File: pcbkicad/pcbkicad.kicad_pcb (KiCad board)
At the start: 2 copper layers, 38 parts, among them J1 USBDaughterboard, U1 AMS1117-3.3, U2 STM32F072CBTx

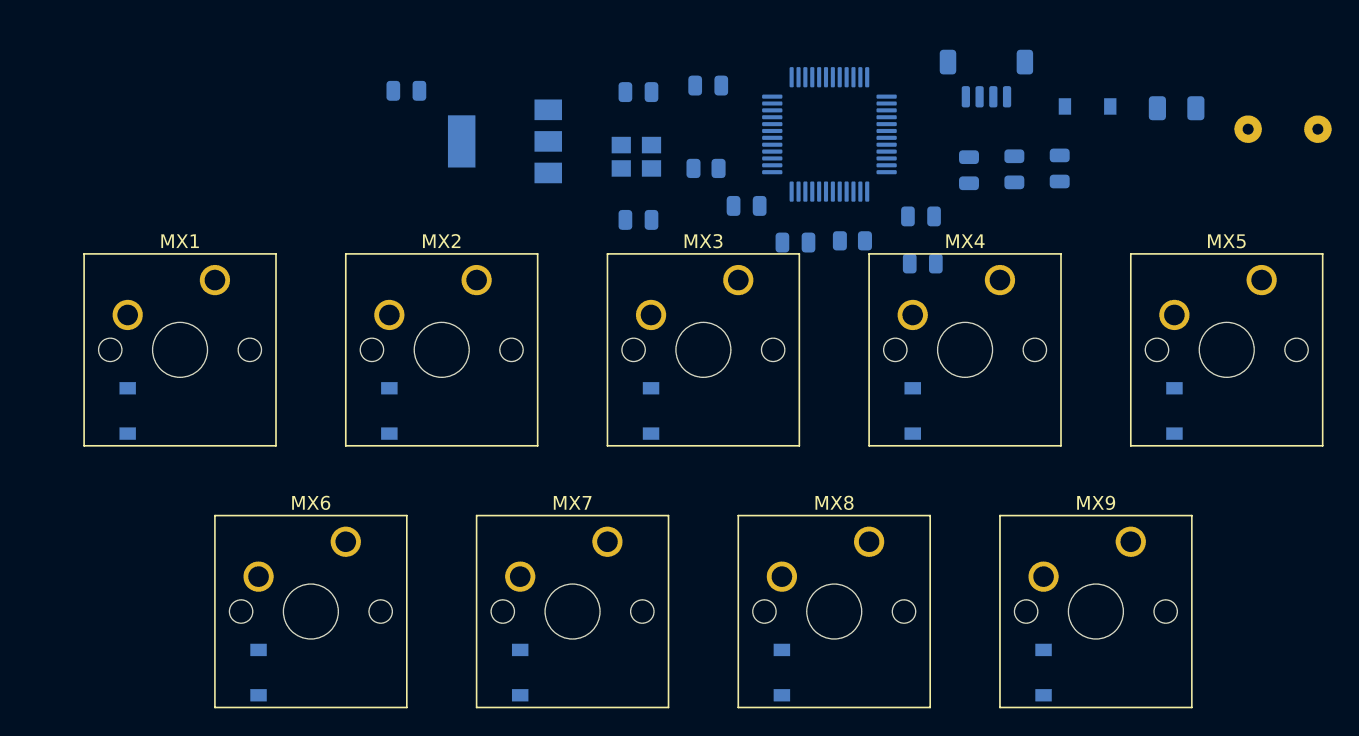
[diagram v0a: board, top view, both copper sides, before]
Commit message: First attempt at routing
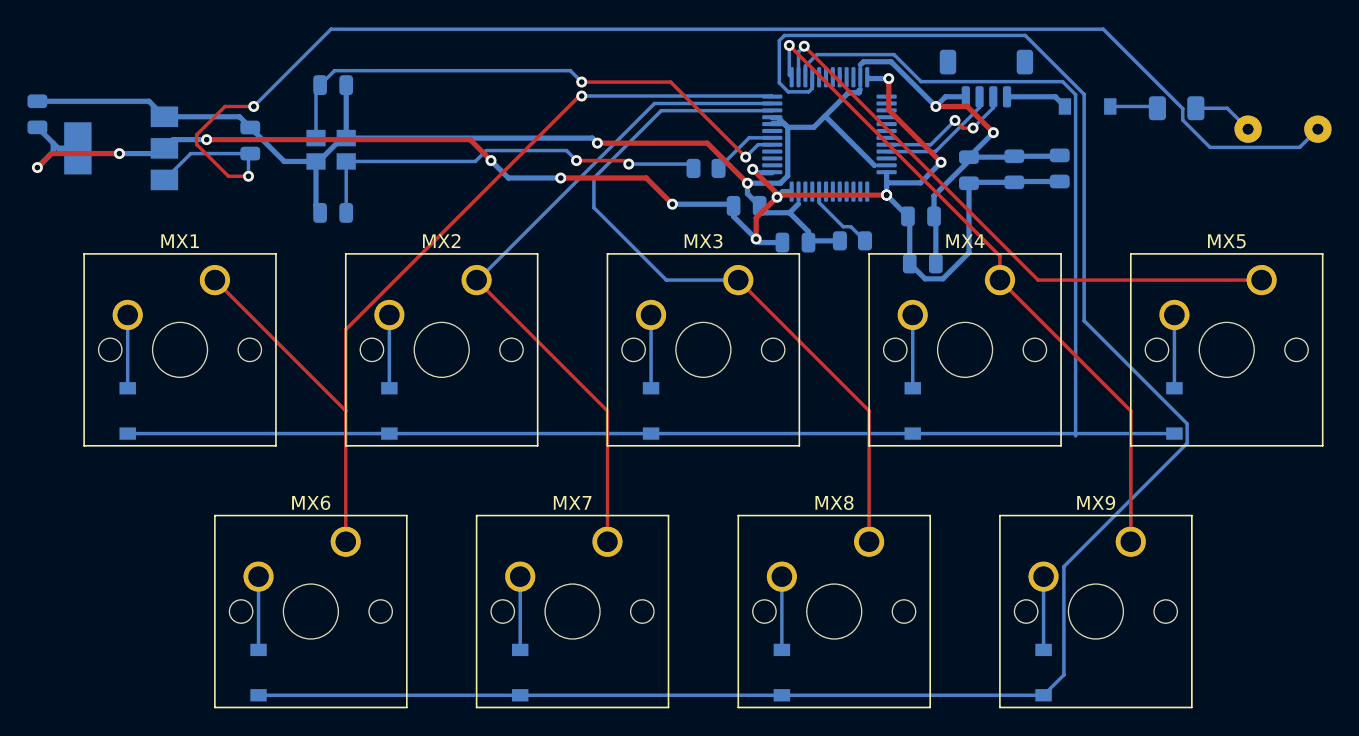
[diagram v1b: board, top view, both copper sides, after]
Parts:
- moved C1 33.6 mm to (93.9, 26.4), turned to 90 degrees
- moved U1 27.9 mm to (84.5, 26.9)
- moved C10 26.9 mm to (78.4, 24.4), turned to 270 degrees
- moved C3 22.2 mm to (99.9, 22.3)
- moved C4 22.2 mm to (99.9, 31.6)
- moved HSE1 22.2 mm to (99.7, 27.0)
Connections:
- U2 pad 10: COL0 -> COL2
- U2 pad 12: COL2 -> COL0
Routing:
- net ROW1: track 0.00 -> 139.1 mm
- net GND: track 0.00 -> 127.3 mm, vias 0 -> 4
- net ROW0: track 0.00 -> 123.1 mm
- net +3V3: track 0.00 -> 121.4 mm, vias 0 -> 13
- net Net-(C1-Pad1): track 0.00 -> 103.6 mm, vias 0 -> 2
- net COL0: track 0.00 -> 67.0 mm, vias 0 -> 1
- net COL2: track 0.00 -> 52.9 mm
- net COL1: track 0.00 -> 49.8 mm
- net COL3: track 0.00 -> 48.8 mm, vias 0 -> 1
- net COL4: track 0.00 -> 42.8 mm, vias 0 -> 1
- net HSE_in: track 0.00 -> 40.3 mm, vias 0 -> 2
- net Net-(C4-Pad1): track 0.00 -> 29.9 mm, vias 0 -> 2
- net D-: track 0.00 -> 10.3 mm, vias 0 -> 2
- net D+: track 0.00 -> 8.87 mm
- net Net-(D9-Pad2): track 0.00 -> 5.34 mm
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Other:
- net class Default: trace_width 0.25 -> 0.254
- net class Power added: clearance 0.2, trace_width 0.381, via_dia 0.8, via_drill 0.4

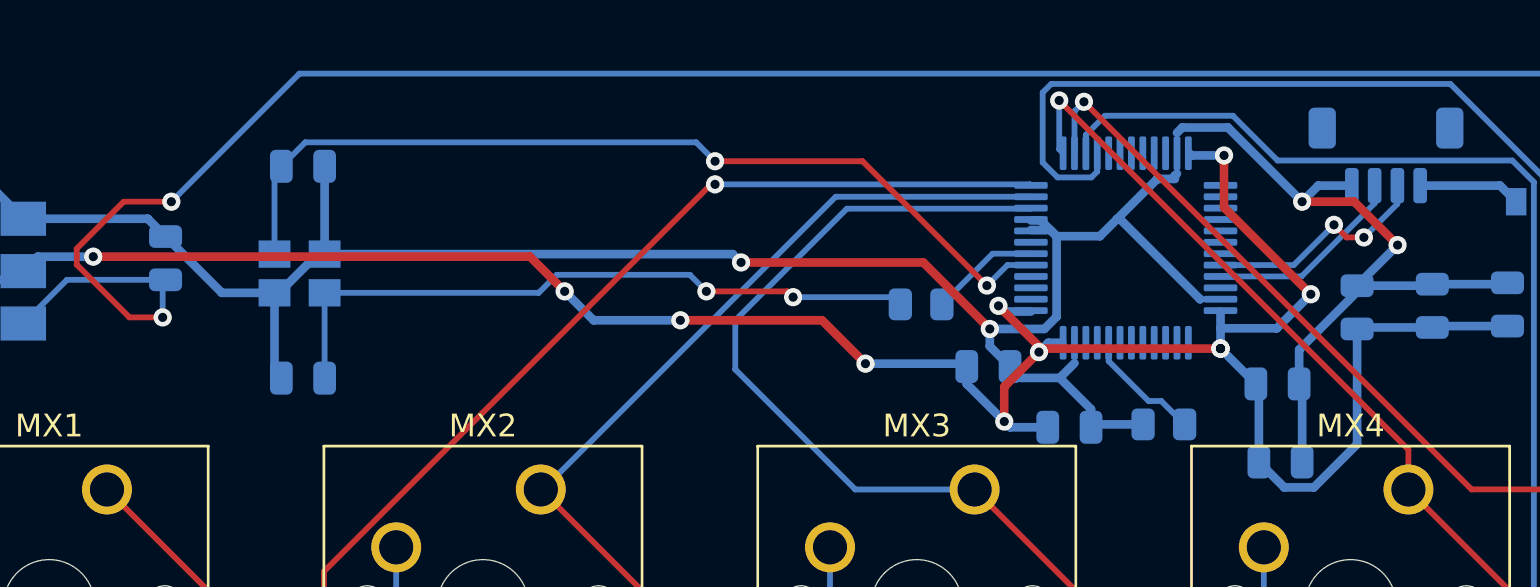
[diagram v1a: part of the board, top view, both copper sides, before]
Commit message: Ground fill
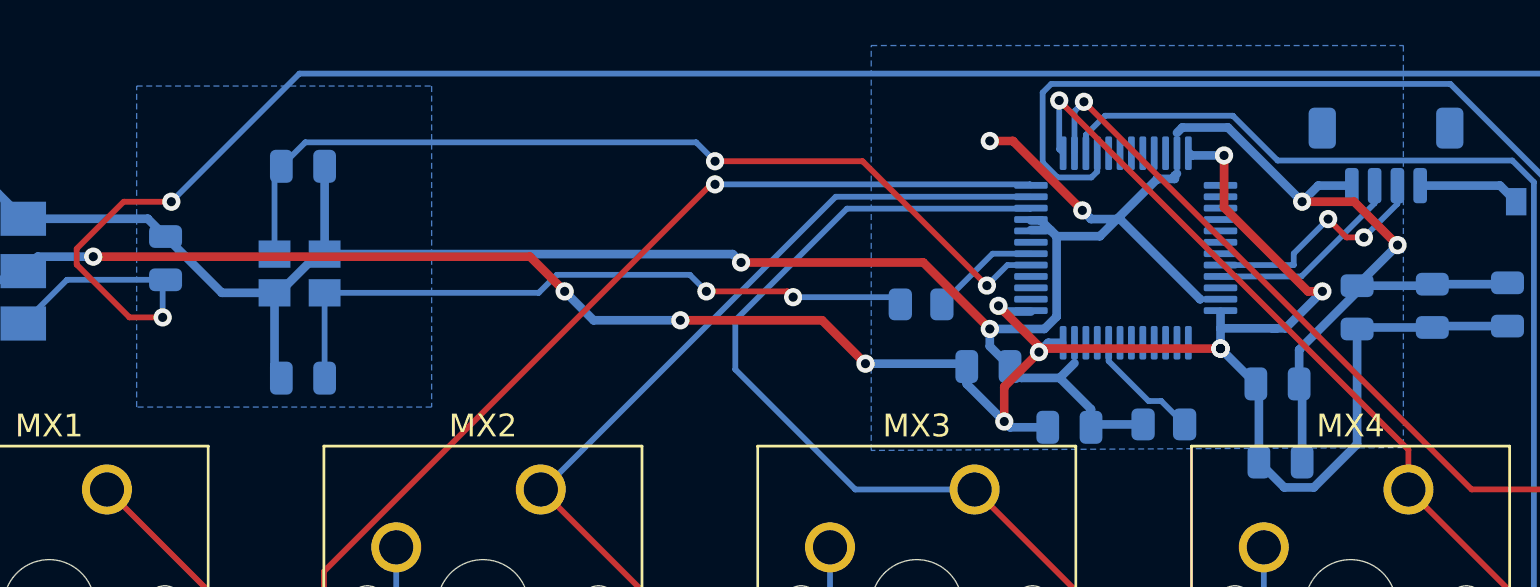
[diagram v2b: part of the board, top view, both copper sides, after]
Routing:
- net GND: track 127.3 -> 134.3 mm, vias 4 -> 6
- net +3V3: track 121.4 -> 122.6 mm
- added copper zone on B.Cu, net GND
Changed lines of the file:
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@@
     (thickness 1.6)
     (drawings 0)
-    (tracks 268)
+    (tracks 278)
     (zones 0)
     (modules 38)
@@
   (segment (start 135.763 24.638) (end 139.283 28.158) (width 0.381) (layer B.Cu) (net 1))
   (segment (start 135.636 24.638) (end 135.763 24.638) (width 0.381) (layer B.Cu) (net 1))
-  (segment (start 134.883822 25.390178) (end 135.636 24.638) (width 0.381) (layer B.Cu) (net 1))
   (segment (start 135.636 24.638) (end 137.40049 22.87351) (width 0.381) (layer B.Cu) (net 1))
   (segment (start 143.764 32.009) (end 143.632 31.877) (width 0.381) (layer B.Cu) (net 1))
@@
   (segment (start 132.290842 24.69851) (end 131.8545 24.69851) (width 0.381) (layer B.Cu) (net 1))
   (segment (start 132.98251 25.390178) (end 132.290842 24.69851) (width 0.381) (layer B.Cu) (net 1))
+  (segment (start 134.883822 25.390178) (end 135.636 24.638) (width 0.381) (layer B.Cu) (net 1))
+  (via (at 134.112 24.257) (size 0.8) (drill 0.4) (layers F.Cu B.Cu) (net 1))
+  (segment (start 134.493 24.638) (end 134.112 24.257) (width 0.381) (layer B.Cu) (net 1))
+  (segment (start 135.636 24.638) (end 134.493 24.638) (width 0.381) (layer B.Cu) (net 1))
+  (via (at 130.048 21.209) (size 0.8) (drill 0.4) (layers F.Cu B.Cu) (net 1))
+  (segment (start 131.064 21.209) (end 130.048 21.209) (width 0.381) (layer F.Cu) (net 1))
+  (segment (start 134.112 24.257) (end 131.064 21.209) (width 0.381) (layer F.Cu) (net 1))
   (segment (start 89.524 27.305) (end 87.605 29.224) (width 0.254) (layer B.Cu) (net 2))
   (segment (start 93.853 27.305) (end 89.524 27.305) (width 0.254) (layer B.Cu) (net 2))
@@
   (segment (start 146.177 34.52382) (end 144.27931 36.42151) (width 0.381) (layer B.Cu) (net 3))
   (segment (start 146.177 29.464) (end 146.177 34.52382) (width 0.381) (layer B.Cu) (net 3))
-  (via (at 144.145 27.94) (size 0.8) (drill 0.4) (layers F.Cu B.Cu) (net 3))
-  (segment (start 142.6495 29.4355) (end 144.145 27.94) (width 0.381) (layer B.Cu) (net 3))
-  (segment (start 140.1795 29.4355) (end 142.6495 29.4355) (width 0.381) (layer B.Cu) (net 3))
+  (via (at 144.653 27.813) (size 0.8) (drill 0.4) (layers F.Cu B.Cu) (net 3))
   (segment (start 140.1795 30.3245) (end 140.1795 29.4355) (width 0.381) (layer B.Cu) (net 3))
   (segment (start 140.1795 29.4355) (end 140.1795 28.69851) (width 0.381) (layer B.Cu) (net 3))
   (via (at 140.335 21.844) (size 0.8) (drill 0.4) (layers F.Cu B.Cu) (net 3))
   (segment (start 140.335 24.13) (end 140.335 21.844) (width 0.381) (layer F.Cu) (net 3))
-  (segment (start 144.145 27.94) (end 140.335 24.13) (width 0.381) (layer F.Cu) (net 3))
   (segment (start 138.90601 21.844) (end 138.80751 21.7455) (width 0.381) (layer B.Cu) (net 3))
   (segment (start 140.335 21.844) (end 138.90601 21.844) (width 0.381) (layer B.Cu) (net 3))
@@
   (segment (start 132.3625 30.3245) (end 132.207 30.48) (width 0.381) (layer F.Cu) (net 3))
   (segment (start 140.1795 30.3245) (end 132.3625 30.3245) (width 0.381) (layer F.Cu) (net 3))
+  (segment (start 143.0305 29.4355) (end 142.4655 29.4355) (width 0.381) (layer B.Cu) (net 3))
+  (segment (start 144.653 27.813) (end 143.0305 29.4355) (width 0.381) (layer B.Cu) (net 3))
+  (segment (start 142.4655 29.4355) (end 142.6495 29.4355) (width 0.381) (layer B.Cu) (net 3))
+  (segment (start 140.1795 29.4355) (end 142.4655 29.4355) (width 0.381) (layer B.Cu) (net 3))
+  (segment (start 144.018 27.813) (end 140.335 24.13) (width 0.381) (layer F.Cu) (net 3))
+  (segment (start 144.653 27.813) (end 144.018 27.813) (width 0.381) (layer F.Cu) (net 3))
   (segment (start 98.638 22.62025) (end 98.938 22.32025) (width 0.254) (layer B.Cu) (net 4))
   (segment (start 98.638 26.1765) (end 98.638 22.62025) (width 0.254) (layer B.Cu) (net 4))
@@
   (segment (start 147.947 23.972134) (end 146.475067 25.444067) (width 0.254) (layer B.Cu) (net 21))
   (segment (start 147.947 23.169) (end 147.947 23.972134) (width 0.254) (layer B.Cu) (net 21))
-  (via (at 145.161 24.892) (size 0.8) (drill 0.4) (layers F.Cu B.Cu) (net 21))
-  (segment (start 145.713067 25.444067) (end 145.034 24.765) (width 0.254) (layer F.Cu) (net 21))
+  (via (at 144.907 24.638) (size 0.8) (drill 0.4) (layers F.Cu B.Cu) (net 21))
   (segment (start 146.475067 25.444067) (end 145.713067 25.444067) (width 0.254) (layer F.Cu) (net 21))
   (segment (start 143.395 26.658) (end 140.1795 26.658) (width 0.254) (layer B.Cu) (net 21))
-  (segment (start 145.161 24.892) (end 143.395 26.658) (width 0.254) (layer B.Cu) (net 21))
+  (segment (start 144.907 24.638) (end 145.713067 25.444067) (width 0.254) (layer F.Cu) (net 21))
+  (segment (start 143.395 26.15) (end 143.395 26.658) (width 0.254) (layer B.Cu) (net 21))
+  (segment (start 144.907 24.638) (end 143.395 26.15) (width 0.254) (layer B.Cu) (net 21))
   (segment (start 100.80625 46.0375) (end 91.28125 36.5125) (width 0.254) (layer F.Cu) (net 22))
   (segment (start 100.80625 55.5625) (end 100.80625 46.0375) (width 0.254) (layer F.Cu) (net 22))
@@
   (segment (start 135.267 30.876528) (end 137.018462 32.62799) (width 0.254) (layer B.Cu) (net 28))
   (segment (start 135.267 30.0705) (end 135.267 30.876528) (width 0.254) (layer B.Cu) (net 28))
+  (zone (net 1) (net_name GND) (layer B.Cu) (hatch edge 0.508)
+    (connect_pads (clearance 0.508))
+    (min_thickness 0.254)
+    (fill yes (arc_segments 32) (thermal_gap 0.508) (thermal_bridge_width 0.508) (smoothing chamfer))
+    (polygon
+      (pts
+        (xy 148.209 34.671) (xy 124.841 34.798) (xy 124.841 17.018) (xy 148.209 17.018)
+      )
+    )
+  )
+  (zone (net 1) (net_name GND) (layer B.Cu) (hatch edge 0.508)
+    (connect_pads (clearance 0.508))
+    (min_thickness 0.254)
+    (fill yes (arc_segments 32) (thermal_gap 0.508) (thermal_bridge_width 0.508) (smoothing chamfer))
+    (polygon
+      (pts
+        (xy 105.537 32.893) (xy 92.583 32.893) (xy 92.583 18.796) (xy 105.537 18.796)
+      )
+    )
+  )
 )

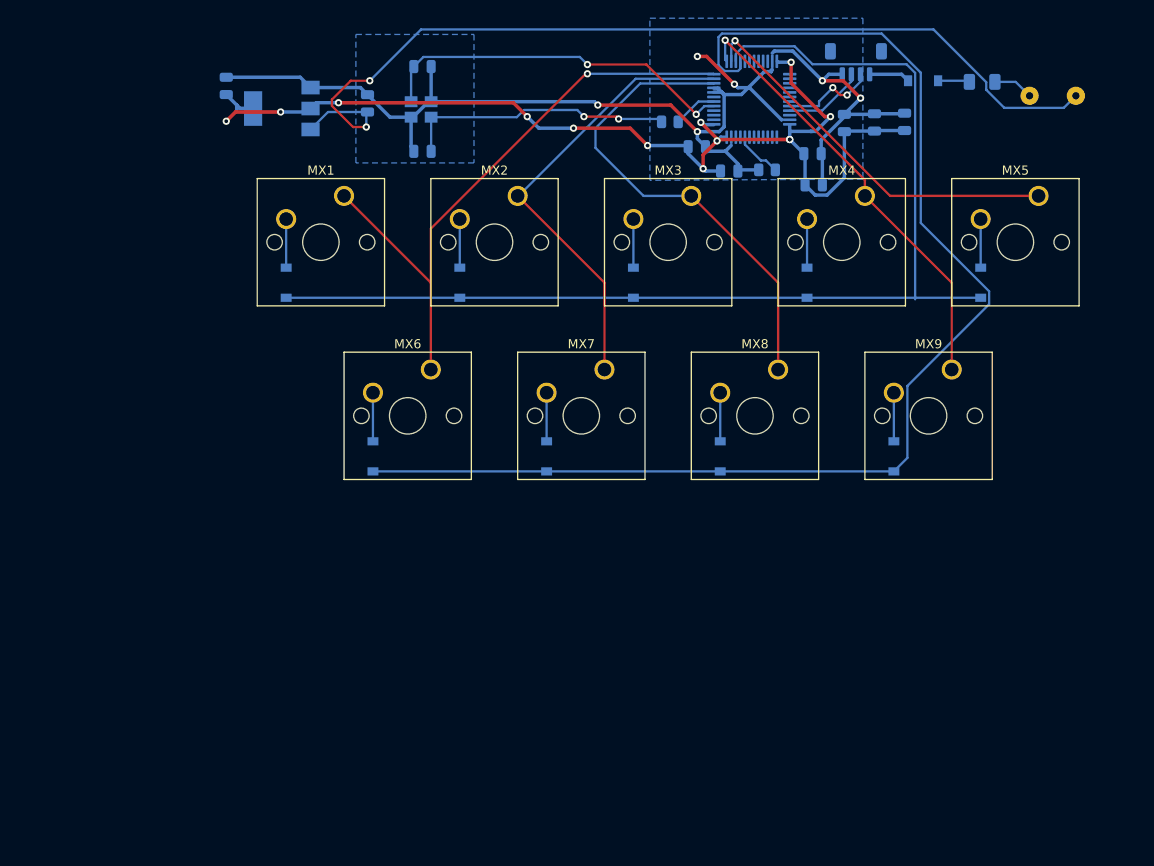
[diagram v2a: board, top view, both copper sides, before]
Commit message: Rerouted and removed unecessary elements
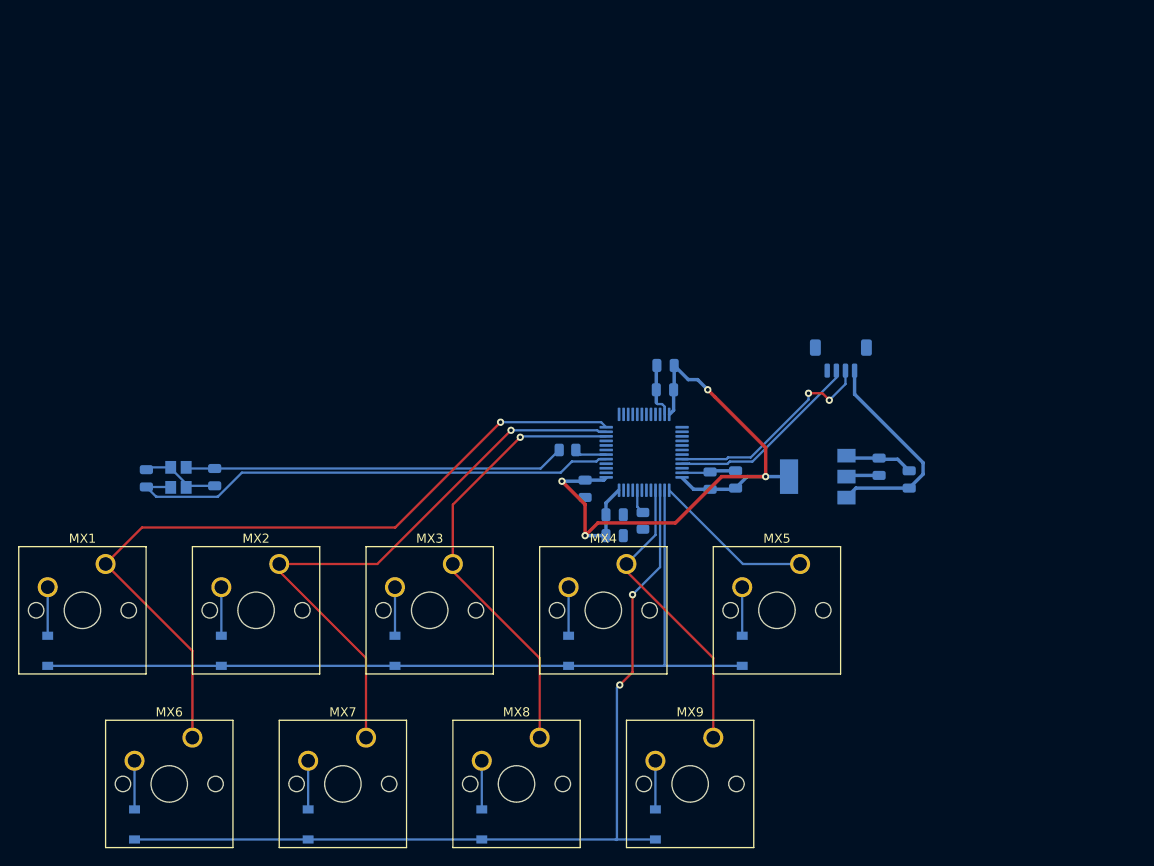
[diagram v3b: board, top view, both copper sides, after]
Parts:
- removed D1: B5819W, Diode_SMD:D_SOD-123
- removed F1: 500 mA, Fuse:Fuse_1206_3216Metric
- removed FB1: 100 @ 100 Mhz, Ferrite_THT:LairdTech_28C0236-0JW-10
- moved C1 72.4 mm to (153.3, 67.6)
- moved U1 71.3 mm to (143.3, 67.3)
- moved C10 68.5 mm to (131.4, 67.8)
- moved C3 54.4 mm to (69.6, 67.5), turned to 90 degrees
- moved C8 53.6 mm to (121.0, 73.8), turned to 180 degrees
- moved C6 49.8 mm to (121.0, 71.5), turned to 180 degrees
- moved HSE1 48.4 mm to (73.1, 67.4), turned to 90 degrees
- moved D2 48.1 mm to (58.8, 86.4)
- moved D3 48.1 mm to (77.8, 86.4)
- moved D4 48.1 mm to (96.9, 86.4)
- moved D5 48.1 mm to (115.9, 86.4)
- moved D6 48.1 mm to (135.0, 86.4)
- moved D9 48.1 mm to (106.4, 105.5)
- moved MX1 48.1 mm to (65.1, 76.9)
- moved MX4 48.1 mm to (122.3, 76.9)
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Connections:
- C1 pad 1: Net-(C1-Pad1) -> VCC
- U1 pad 3: Net-(C1-Pad1) -> VCC
- U2 pad 13: COL3 -> Net-(U2-Pad13)
- U2 pad 14: COL4 -> Net-(U2-Pad14)
- U2 pad 15: ROW0 -> Net-(U2-Pad15)
- U2 pad 16: ROW1 -> Net-(U2-Pad16)
- U2 pad 37: Net-(U2-Pad37) -> COL4
- U2 pad 38: Net-(U2-Pad38) -> ROW0
- U2 pad 39: Net-(U2-Pad39) -> ROW1
- U2 pad 40: Net-(U2-Pad40) -> COL3
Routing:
- net GND: track 134.3 -> 28.5 mm, vias 6 -> 0
- net Net-(C1-Pad1): track 103.6 -> 0.00 mm, vias 2 -> 0
- net ROW1: track 139.1 -> 97.5 mm, vias 0 -> 2
- net +3V3: track 122.6 -> 81.4 mm, vias 13 -> 4
- net ROW0: track 123.1 -> 95.5 mm
- net COL4: track 42.8 -> 17.7 mm, vias 1 -> 0
- net VCC: track 4.51 -> 24.0 mm
- net COL0: track 67.0 -> 84.6 mm
- net COL3: track 48.8 -> 32.4 mm, vias 1 -> 0
- net COL1: track 49.8 -> 65.0 mm, vias 0 -> 1
- net HSE_in: track 40.3 -> 55.3 mm, vias 2 -> 0
- net D-: track 10.6 -> 23.9 mm
- net D+: track 8.87 -> 21.6 mm
- net Net-(C4-Pad1): track 29.9 -> 41.8 mm, vias 2 -> 0
- net Net-(F1-Pad1): track 4.44 -> 0.00 mm
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- removed copper zone on B.Cu, net GND

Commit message: Schematic protection
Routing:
- net GND: track 28.5 -> 47.8 mm
- net +3V3: track 81.4 -> 87.7 mm

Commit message: I honestly don't remember
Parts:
- added D1: D_TVS, Diode_SMD:D_0201_0603Metric, F.Cu at (171.7, 69.0)
- added F1: 500 mA, Fuse:Fuse_0402_1005Metric, F.Cu at (167.3, 70.9)
- added R3: 5.1k, Resistor_SMD:R_0805_2012Metric, B.Cu at (166.6, 53.5)
- added R4: 5.1k, Resistor_SMD:R_0805_2012Metric, F.Cu at (168.0, 68.5)
- added U3: TPD4E02B04DQA, Package_SON:USON-10_2.5x1.0mm_P0.5mm, B.Cu at (173.4, 52.1)
- J1: value USBDaughterboard -> USB_C_Receptacle_USB2.0; footprint Connector_JST:JST_SH_BM04B-SRSS-TB_1x04-1MP_P1.00mm_Vertical -> Connector_USB:USB_C_Receptacle_HRO_TYPE-C-31-M-12
- moved J1 29.0 mm to (173.4, 45.3), turned to 0 degrees
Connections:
- C1 pad 1: VCC -> Net-(C1-Pad1)
- C1 pad 2: GND -> +3V3
- C10 pad 1: GND -> +3V3
- C11 pad 1: GND -> +3V3
- C2 pad 2: GND -> +3V3
- C3 pad 2: GND -> +3V3
- C4 pad 2: GND -> +3V3
- C5 pad 1: GND -> +3V3
- C6 pad 1: GND -> +3V3
- C7 pad 1: GND -> +3V3
- C8 pad 1: GND -> +3V3
- C9 pad 1: GND -> +3V3
- HSE1 pad 2: GND -> +3V3
- HSE1 pad 4: GND -> +3V3
- R2 pad 2: GND -> +3V3
- U1 pad 1: GND -> +3V3
- U1 pad 3: VCC -> Net-(C1-Pad1)
- U2 pad 23: GND -> +3V3
- U2 pad 35: GND -> +3V3
- U2 pad 47: GND -> +3V3
- U2 pad 8: GND -> +3V3
- U2 pad 9: GND -> Net-(U2-Pad9)
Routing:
- net VCC: track 24.0 -> 0.00 mm
- net Net-(C1-Pad1): track 0.00 -> 21.4 mm
- net +3V3: track 87.7 -> 104.1 mm
- net GND: track 47.8 -> 31.3 mm
- net D-: track 23.9 -> 16.6 mm, vias 2 -> 0
- net D+: track 21.6 -> 20.9 mm
